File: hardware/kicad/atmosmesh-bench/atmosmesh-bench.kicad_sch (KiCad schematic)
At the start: 24 parts, among them J1 LCD1602_I2C, J2 GY-BMP280, J3 AM2302, J4 SDS011, J5 MQ135, J6 5V_IN, J7 ESP32_Harness, U1 ESP32_DevKit_V1_Socket

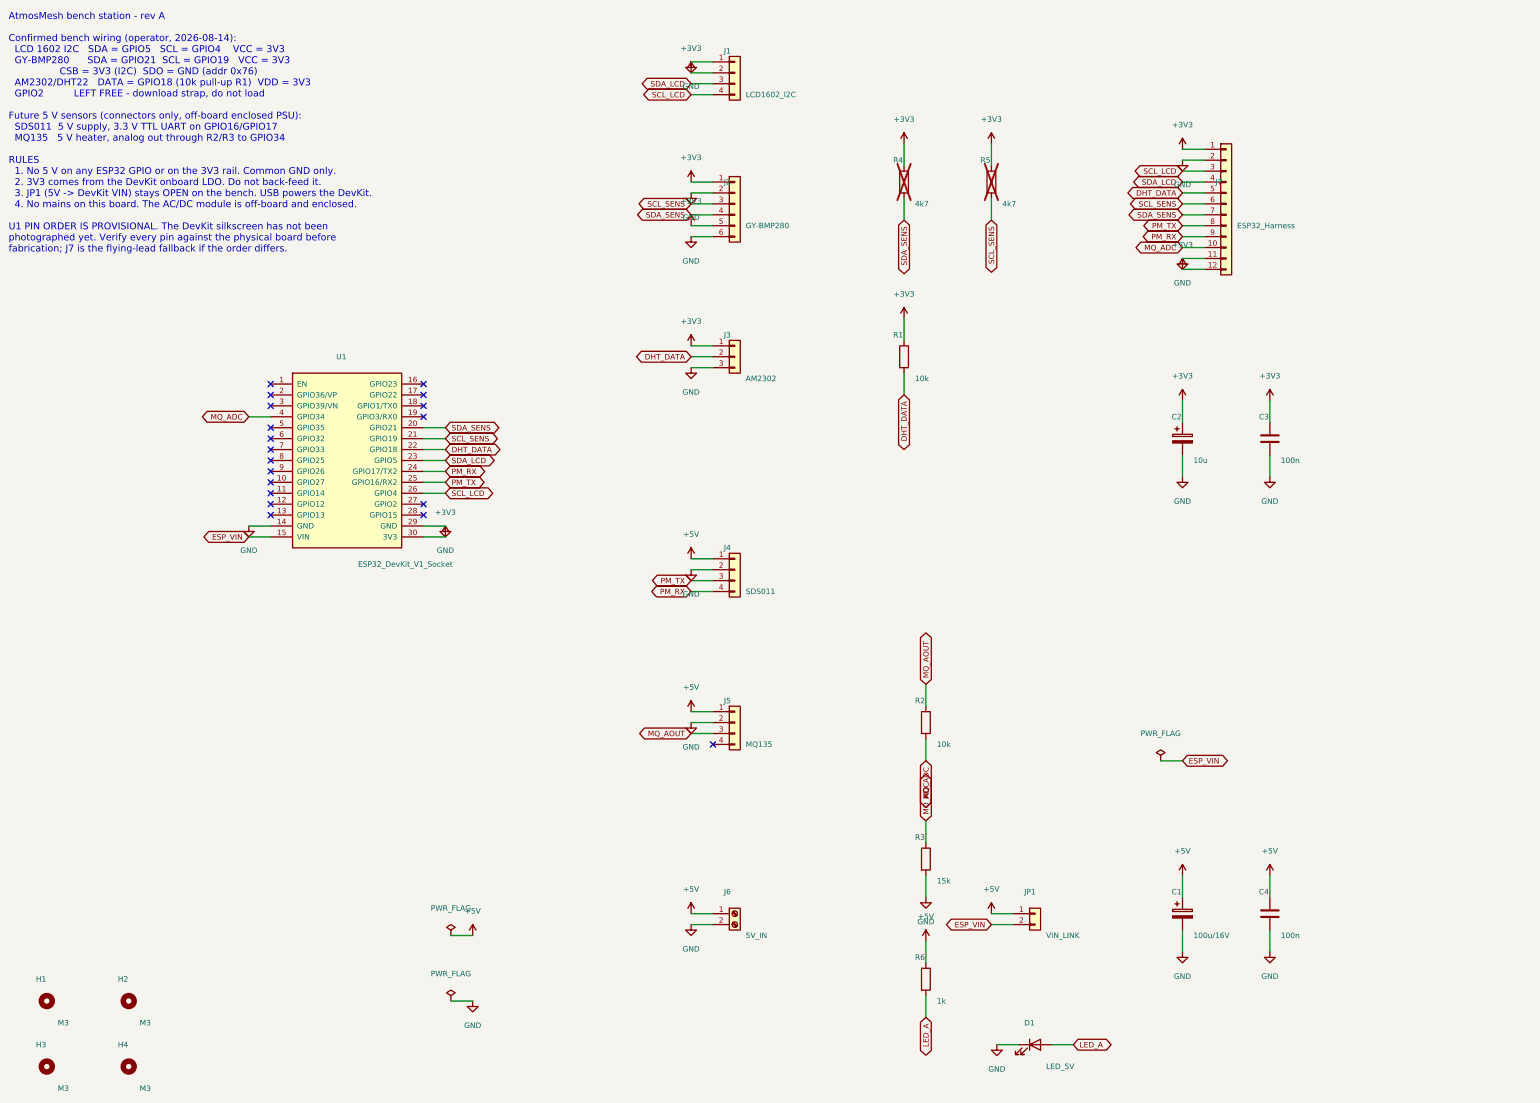
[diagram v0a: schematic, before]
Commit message: :sparkles: feat(pcb): add extras headers and route the bench board
J_BEEP/J_PIR/J_VEML, 139 mm outline, and a fully routed copper pour.
Ignore KiCad .history and restore snapshots so they stay local.
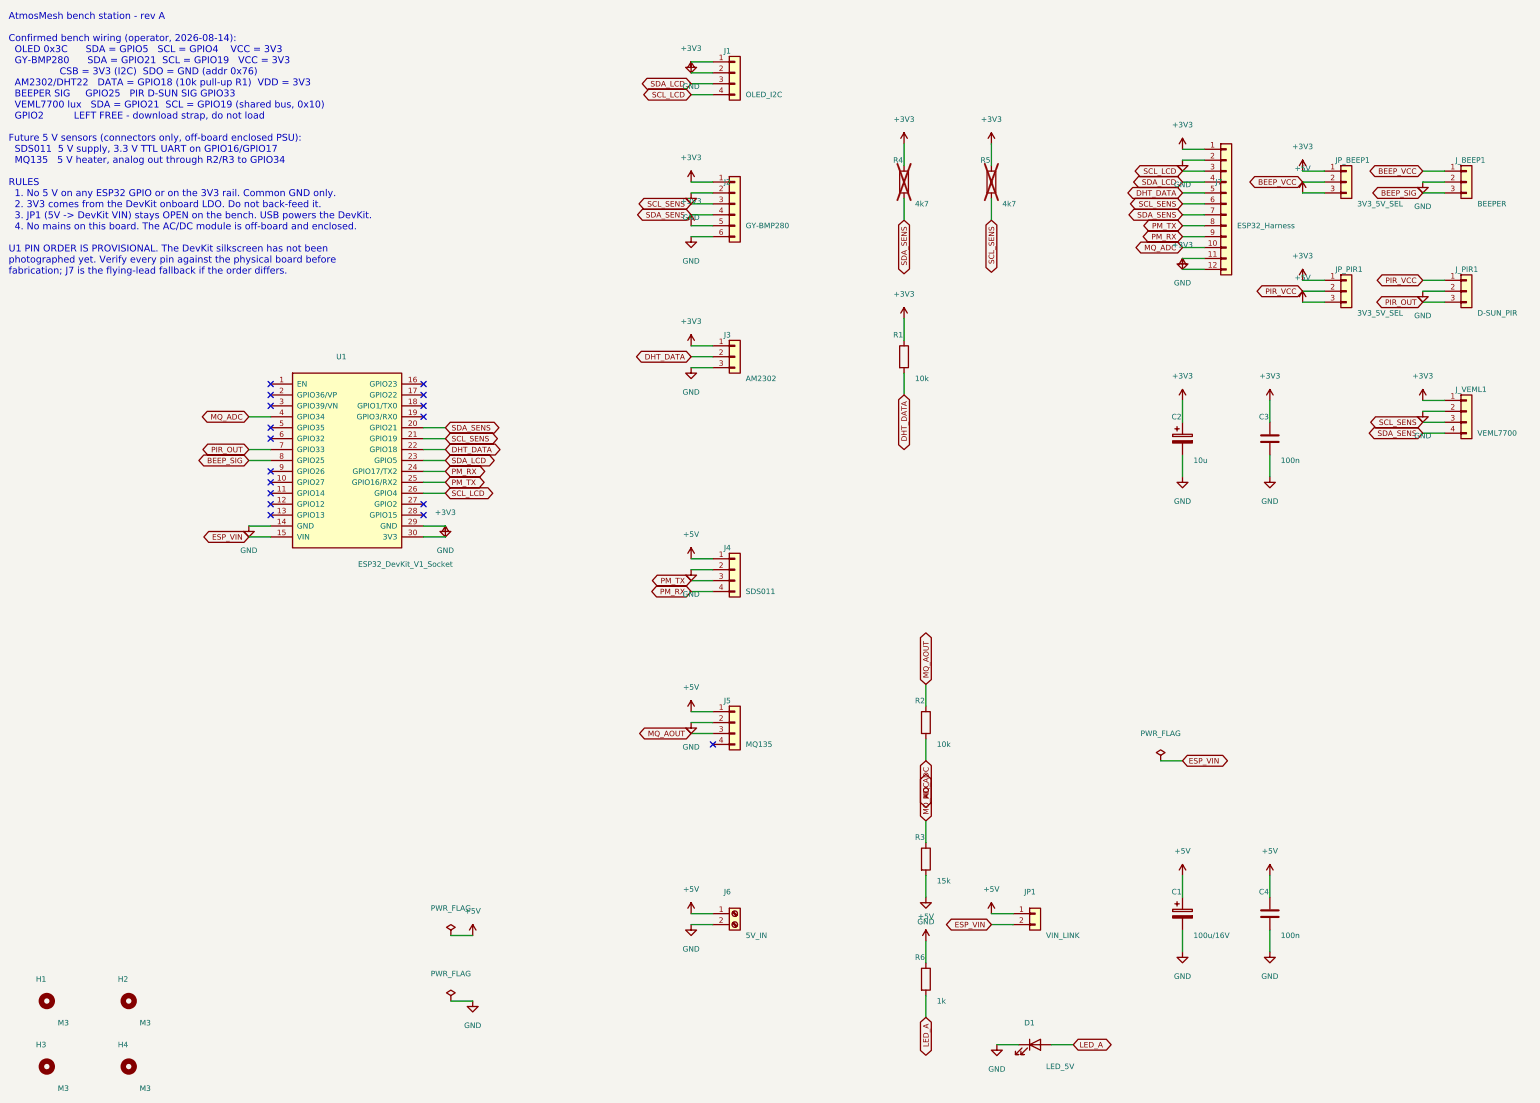
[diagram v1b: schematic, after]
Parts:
- added JP_BEEP1, JP_PIR1: 3V3_5V_SEL, atmosmesh:PinHeader_1x03_P2.54mm_Vertical, symbol atmosmesh:Conn_01x03
- added J_BEEP1: BEEPER, atmosmesh:PinHeader_1x03_P2.54mm_Vertical, symbol atmosmesh:Conn_01x03
- added J_PIR1: D-SUN_PIR, atmosmesh:PinHeader_1x03_P2.54mm_Vertical, symbol atmosmesh:Conn_01x03
- added J_VEML1: VEML7700, atmosmesh:PinHeader_1x04_P2.54mm_Vertical, symbol atmosmesh:Conn_01x04
- J1: value LCD1602_I2C -> OLED_I2C
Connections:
- net +3V3: now also JP_BEEP1.1 (Pin_1), JP_PIR1.1 (Pin_1), J_VEML1.1 (Pin_1)
- net +5V: now also JP_BEEP1.3 (Pin_3), JP_PIR1.3 (Pin_3)
- net GND: now also J_BEEP1.2 (Pin_2), J_PIR1.2 (Pin_2), J_VEML1.2 (Pin_2)
- net SCL_SENS: now also J_VEML1.3 (Pin_3)
- net SDA_SENS: now also J_VEML1.4 (Pin_4)
- net PIR_OUT: now reaches U1.7 (GPIO33)
- net PIR_OUT: now also J_PIR1.3 (Pin_3)
- net BEEP_SIG: now reaches U1.8 (GPIO25)
- net BEEP_SIG: now also J_BEEP1.3 (Pin_3)
- new net BEEP_VCC: JP_BEEP1.2 (Pin_2), J_BEEP1.1 (Pin_1)
- new net PIR_VCC: JP_PIR1.2 (Pin_2), J_PIR1.1 (Pin_1)
- no-connect marks 19 -> 17
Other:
- note added: "AtmosMesh bench station - rev A Confirmed bench wiring (operator, 2026-08-14): OLED 0x3C SDA = GPIO5 SCL = GPIO4 VCC = 3V3 GY-BMP280 SDA = GPIO21 SCL = GPIO19 VCC = 3V3 CSB = 3V3 (I2C) SDO = GND (addr 0x76) AM2302/DHT22 DATA = GPIO18 (10k pull-up R1) VDD = 3V3 BEEPER SIG GPIO25 PIR D-SUN SIG GPIO33 VEML7700 lux SDA = GPIO21 SCL = GPIO19 (shared bus, 0x10) GPIO2 LEFT FREE - download strap, do not 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"
- note removed: "AtmosMesh bench station - rev A Confirmed bench wiring (operator, 2026-08-14): LCD 1602 I2C SDA = GPIO5 SCL = GPIO4 VCC = 3V3 GY-BMP280 SDA = GPIO21 SCL = GPIO19 VCC = 3V3 CSB = 3V3 (I2C) SDO = GND (addr 0x76) AM2302/DHT22 DATA = GPIO18 (10k pull-up R1) VDD = 3V3 GPIO2 LEFT FREE - download strap, do not load Future 5 V sensors (connectors only, off-board enclosed PSU): SDS011 5 V supply, 3.3 V TT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"
